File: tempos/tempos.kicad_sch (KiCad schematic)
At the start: 8 parts

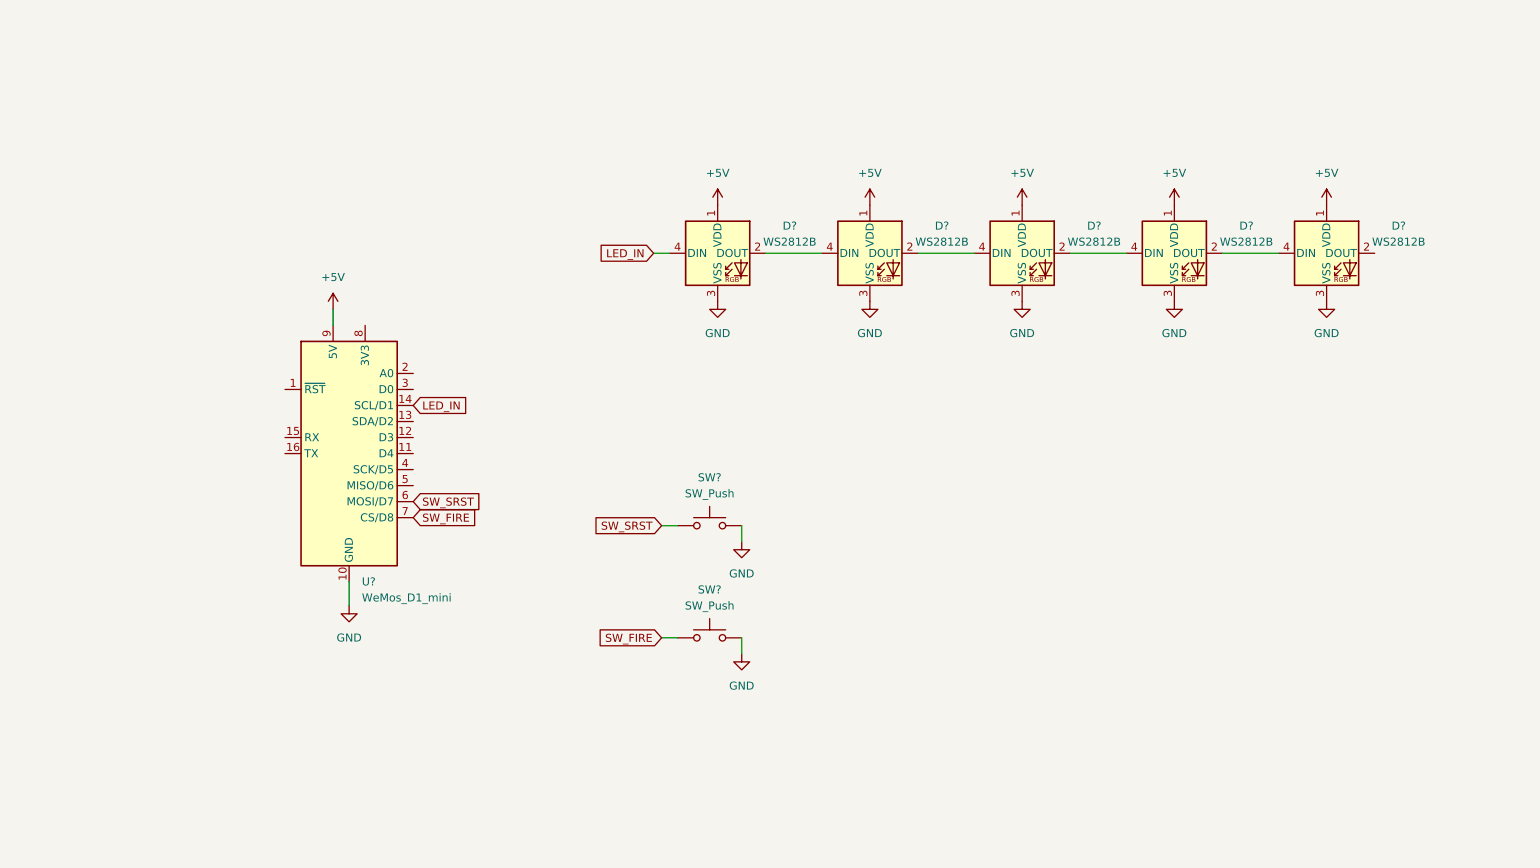
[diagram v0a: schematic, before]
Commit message: tempos: Transmission wire
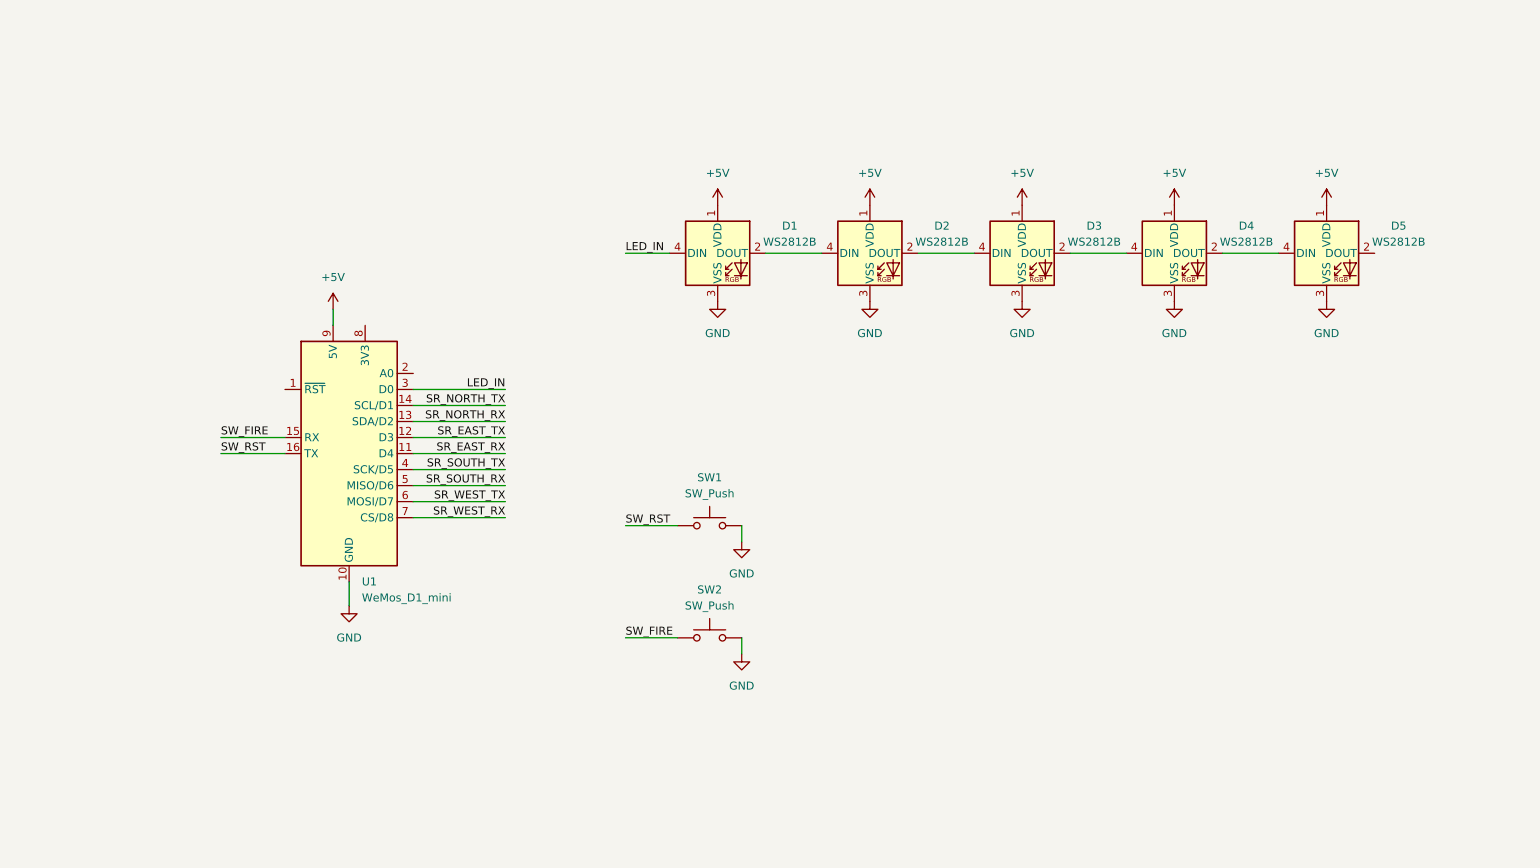
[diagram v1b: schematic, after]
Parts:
- gave numbers to parts that had none: 8
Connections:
- net LED_IN: now also U1.3 (D0); no longer U1.14 (SCL/D1)
- net SW_FIRE: now also U1.15 (RX); no longer U1.7 (CS/D8)
- net SR_EAST_RX: now reaches U1.11 (D4)
- net SR_EAST_TX: now reaches U1.12 (D3)
- net SR_NORTH_RX: now reaches U1.13 (SDA/D2)
- net SW_RST: now reaches U1.16 (TX)
- net SW_RST: now also SW1.1
- net SR_SOUTH_TX: now reaches U1.4 (SCK/D5)
- net SR_SOUTH_RX: now reaches U1.5 (MISO/D6)
- net SW_SRST renamed SR_WEST_TX
- net SR_WEST_TX: no longer SW1.1
- new net SR_NORTH_TX: U1.14 (SCL/D1)
- new net SR_WEST_RX: U1.7 (CS/D8)

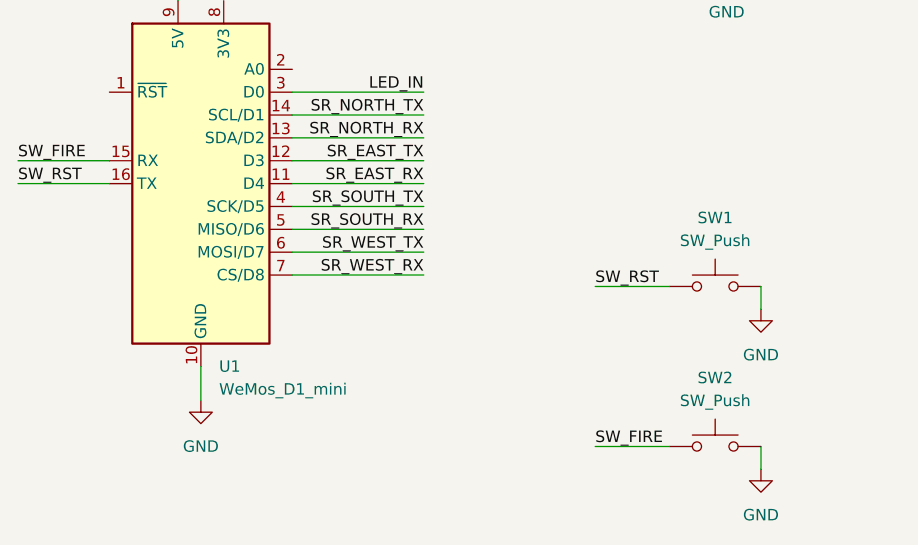
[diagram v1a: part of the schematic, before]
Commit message: tempos: Text description for the switches
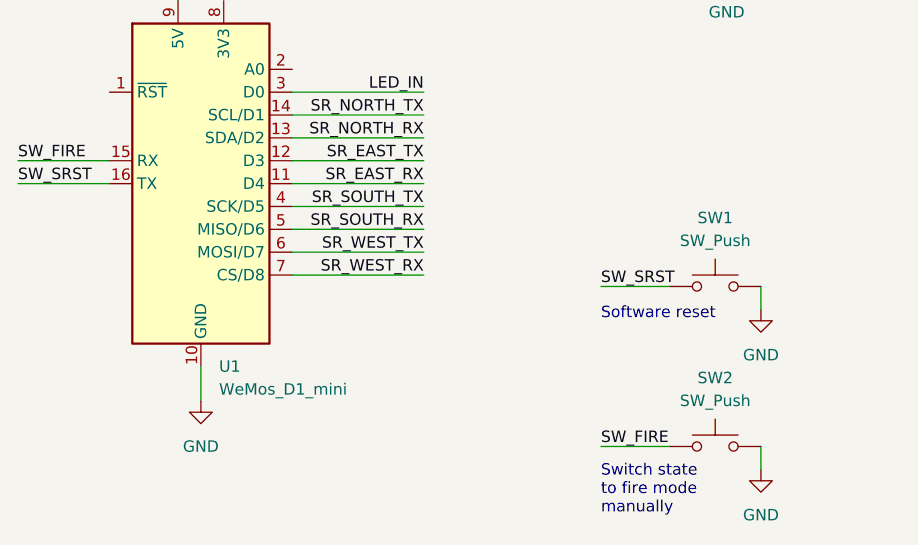
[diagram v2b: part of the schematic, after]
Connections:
- net SW_RST renamed SW_SRST
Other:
- note added: "Software reset"
- note added: "Switch state to fire mode manually"
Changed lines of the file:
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@@
     (stroke (width 0) (type default) (color 0 0 0 0))
   )
-  (wire (pts (xy 130.175 107.95) (xy 138.43 107.95))
+  (wire (pts (xy 130.81 107.95) (xy 138.43 107.95))
     (stroke (width 0) (type default) (color 0 0 0 0))
   )
@@
     (stroke (width 0) (type default) (color 0 0 0 0))
   )
-  (wire (pts (xy 130.175 125.73) (xy 138.43 125.73))
+  (wire (pts (xy 130.81 125.73) (xy 138.43 125.73))
     (stroke (width 0) (type default) (color 0 0 0 0))
+  )
+  (text "Switch state\nto fire mode\nmanually" (at 130.81 133.35 0)
+    (effects (font (size 1.27 1.27)) (justify left bottom))
+  )
+  (text "Software reset" (at 130.81 111.76 0)
+    (effects (font (size 1.27 1.27)) (justify left bottom))
   )
   (label "SR_WEST_TX" (at 111.125 104.14 180)
@@
     (effects (font (size 1.27 1.27)) (justify right bottom))
   )
-  (label "SW_RST" (at 66.04 96.52 0)
+  (label "SW_SRST" (at 66.04 96.52 0)
     (effects (font (size 1.27 1.27)) (justify left bottom))
   )
@@
     (effects (font (size 1.27 1.27)) (justify right bottom))
   )
-  (label "SW_FIRE" (at 130.175 125.73 0)
+  (label "SW_FIRE" (at 130.81 125.73 0)
     (effects (font (size 1.27 1.27)) (justify left bottom))
   )
@@
     (effects (font (size 1.27 1.27)) (justify right bottom))
   )
-  (label "SW_RST" (at 130.175 107.95 0)
+  (label "SW_SRST" (at 130.81 107.95 0)
     (effects (font (size 1.27 1.27)) (justify left bottom))
   )

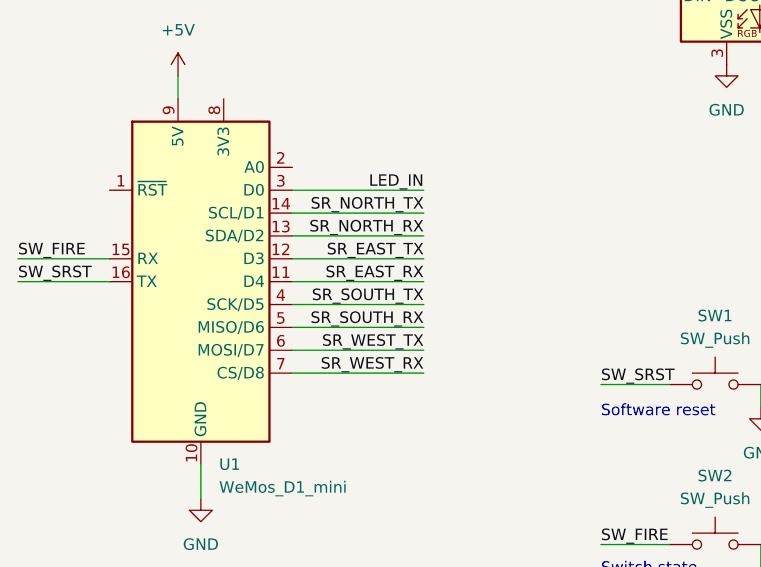
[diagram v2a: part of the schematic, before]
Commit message: tempos: Rearrange RX/TX pins
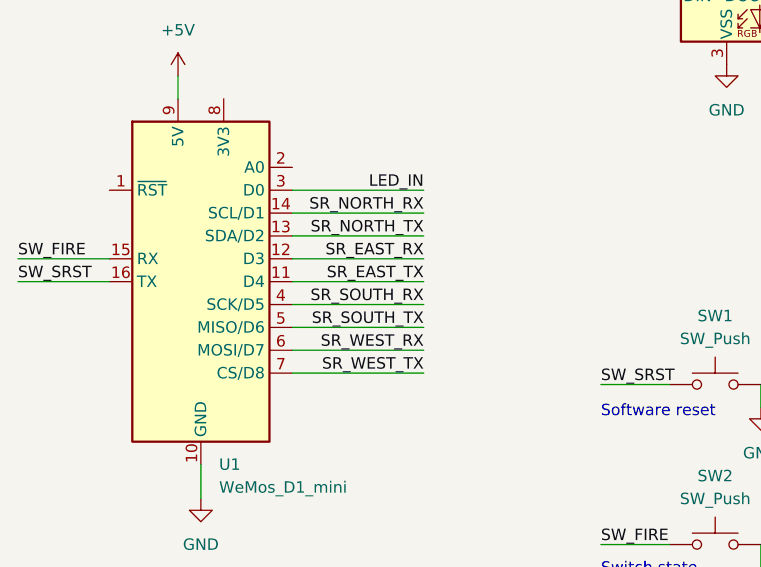
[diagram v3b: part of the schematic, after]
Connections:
- net SR_EAST_RX: now also U1.12 (D3); no longer U1.11 (D4)
- net SR_EAST_TX: now also U1.11 (D4); no longer U1.12 (D3)
- net SR_NORTH_RX: now also U1.14 (SCL/D1); no longer U1.13 (SDA/D2)
- net SR_NORTH_TX: now also U1.13 (SDA/D2); no longer U1.14 (SCL/D1)
- net SR_SOUTH_RX: now also U1.4 (SCK/D5); no longer U1.5 (MISO/D6)
- net SR_SOUTH_TX: now also U1.5 (MISO/D6); no longer U1.4 (SCK/D5)
- net SR_WEST_RX: now also U1.6 (MOSI/D7); no longer U1.7 (CS/D8)
- net SR_WEST_TX: now also U1.7 (CS/D8); no longer U1.6 (MOSI/D7)
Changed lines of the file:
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@@
     (effects (font (size 1.27 1.27)) (justify left bottom))
   )
-  (label "SR_WEST_TX" (at 111.125 104.14 180)
+  (label "SR_WEST_RX" (at 111.125 104.14 180)
     (effects (font (size 1.27 1.27)) (justify right bottom))
   )
-  (label "SR_EAST_TX" (at 111.125 93.98 180)
+  (label "SR_EAST_RX" (at 111.125 93.98 180)
     (effects (font (size 1.27 1.27)) (justify right bottom))
   )
-  (label "SR_NORTH_RX" (at 111.125 91.44 180)
+  (label "SR_NORTH_TX" (at 111.125 91.44 180)
     (effects (font (size 1.27 1.27)) (justify right bottom))
   )
@@
     (effects (font (size 1.27 1.27)) (justify left bottom))
   )
-  (label "SR_WEST_RX" (at 111.125 106.68 180)
+  (label "SR_WEST_TX" (at 111.125 106.68 180)
     (effects (font (size 1.27 1.27)) (justify right bottom))
   )
@@
     (effects (font (size 1.27 1.27)) (justify left bottom))
   )
-  (label "SR_SOUTH_TX" (at 111.125 99.06 180)
+  (label "SR_SOUTH_RX" (at 111.125 99.06 180)
     (effects (font (size 1.27 1.27)) (justify right bottom))
   )
-  (label "SR_NORTH_TX" (at 111.125 88.9 180)
+  (label "SR_NORTH_RX" (at 111.125 88.9 180)
     (effects (font (size 1.27 1.27)) (justify right bottom))
   )
@@
     (effects (font (size 1.27 1.27)) (justify left bottom))
   )
-  (label "SR_EAST_RX" (at 111.125 96.52 180)
+  (label "SR_EAST_TX" (at 111.125 96.52 180)
     (effects (font (size 1.27 1.27)) (justify right bottom))
   )
-  (label "SR_SOUTH_RX" (at 111.125 101.6 180)
+  (label "SR_SOUTH_TX" (at 111.125 101.6 180)
     (effects (font (size 1.27 1.27)) (justify right bottom))
   )

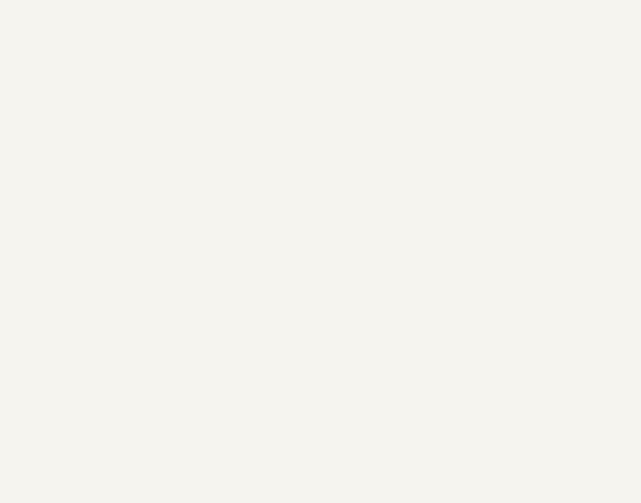
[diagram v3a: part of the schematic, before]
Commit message: hardware: Circuit diagram for six nodes  Connected RX/TX pins together between six nodes.
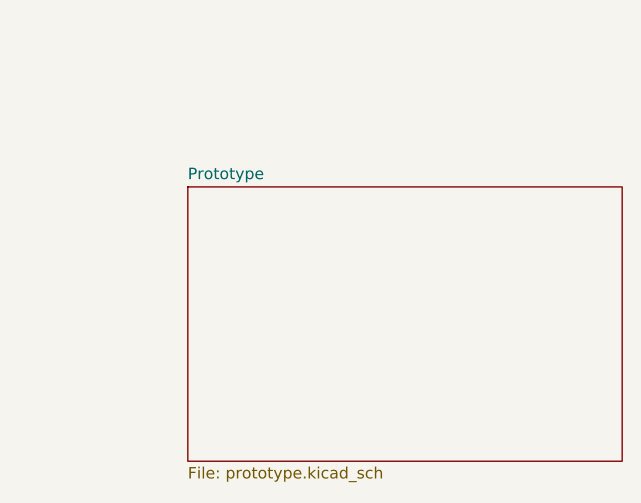
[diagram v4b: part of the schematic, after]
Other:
- added sheet Prototype (prototype.kicad_sch)
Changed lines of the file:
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@@
     (pin "2")
+  )
+  (sheet (at 224.79 127) (size 48.26 30.48) (fields_autoplaced)
+    (stroke (width 0.1524) (type solid) (color 0 0 0 0))
+    (fill (color 0 0 0 0.0000))
+    (property "Sheet name" "Prototype" (id 0) (at 224.79 126.2884 0)
+      (effects (font (size 1.27 1.27)) (justify left bottom))
+    )
+    (property "Sheet file" "prototype.kicad_sch" (id 1) (at 224.79 158.0646 0)
+      (effects (font (size 1.27 1.27)) (justify left top))
+    )
   )
   (sheet_instances
     (path "/" (page "1"))
+    (path "/2c19c399-c4f7-40ce-804e-49fc3383ca4e" (page "2"))
   )
   (symbol_instances
@@
       (reference "#PWR014") (unit 1) (value "GND") (footprint "")
     )
+    (path "/2c19c399-c4f7-40ce-804e-49fc3383ca4e/3c29d72d-e391-4942-8469-a1a227f3d93d"
+      (reference "#PWR?") (unit 1) (value "GND") (footprint "")
+    )
+    (path "/2c19c399-c4f7-40ce-804e-49fc3383ca4e/3d046c0b-d445-4332-a8e3-cad08dc3d7a5"
+      (reference "#PWR?") (unit 1) (value "GND") (footprint "")
+    )
+    (path "/2c19c399-c4f7-40ce-804e-49fc3383ca4e/4f84264e-389c-4cb3-b1ef-b18c33e26c32"
+      (reference "#PWR?") (unit 1) (value "GND") (footprint "")
+    )
+    (path "/2c19c399-c4f7-40ce-804e-49fc3383ca4e/684ab4bf-d763-4862-8762-c7424275837e"
+      (reference "#PWR?") (unit 1) (value "+3.3V") (footprint "")
+    )
+    (path "/2c19c399-c4f7-40ce-804e-49fc3383ca4e/6ef3b29a-ee7a-4b63-81c1-ce6ddc24bb1c"
+      (reference "#PWR?") (unit 1) (value "GND") (footprint "")
+    )
+    (path "/2c19c399-c4f7-40ce-804e-49fc3383ca4e/6f3c1782-d190-44d6-b32b-e4547d6c973b"
+      (reference "#PWR?") (unit 1) (value "+3.3V") (footprint "")
+    )
+    (path "/2c19c399-c4f7-40ce-804e-49fc3383ca4e/7c97b1c9-4321-4174-981f-9646edd3dcd6"
+      (reference "#PWR?") (unit 1) (value "+3.3V") (footprint "")
+    )
+    (path "/2c19c399-c4f7-40ce-804e-49fc3383ca4e/98a4c6aa-259e-4081-9383-2e60646be403"
+      (reference "#PWR?") (unit 1) (value "+3.3V") (footprint "")
+    )
+    (path "/2c19c399-c4f7-40ce-804e-49fc3383ca4e/bb7f49a8-37a0-4430-adfe-10237aaa0106"
+      (reference "#PWR?") (unit 1) (value "+3.3V") (footprint "")
+    )
+    (path "/2c19c399-c4f7-40ce-804e-49fc3383ca4e/bcbec452-6f24-4fa2-bcf6-898df827344a"
+      (reference "#PWR?") (unit 1) (value "+3.3V") (footprint "")
+    )
+    (path "/2c19c399-c4f7-40ce-804e-49fc3383ca4e/fa4fd627-4259-4330-bbdf-3673be9bdffd"
+      (reference "#PWR?") (unit 1) (value "GND") (footprint "")
+    )
+    (path "/2c19c399-c4f7-40ce-804e-49fc3383ca4e/fe72663a-120a-4556-9cd5-6bd60258b464"
+      (reference "#PWR?") (unit 1) (value "GND") (footprint "")
+    )
     (path "/eb30ba93-4b30-413b-b3b4-5dbe10cd6f18"
       (reference "D1") (unit 1) (value "WS2812B") (footprint "")
@@
       (reference "U1") (unit 1) (value "WeMos_D1_mini") (footprint "Module:WEMOS_D1_mini_light")
     )
+    (path "/2c19c399-c4f7-40ce-804e-49fc3383ca4e/2ac05e0a-a519-4fbd-a00c-2a5e9f9d000c"
+      (reference "U?") (unit 1) (value "WeMos_D1_mini") (footprint "Module:WEMOS_D1_mini_light")
+    )
+    (path "/2c19c399-c4f7-40ce-804e-49fc3383ca4e/3e6f4211-8543-4b21-8501-727ffb144cf7"
+      (reference "U?") (unit 1) (value "WeMos_D1_mini") (footprint "Module:WEMOS_D1_mini_light")
+    )
+    (path "/2c19c399-c4f7-40ce-804e-49fc3383ca4e/8721c7ed-7c2e-44cf-992d-79845ff9e4f2"
+      (reference "U?") (unit 1) (value "WeMos_D1_mini") (footprint "Module:WEMOS_D1_mini_light")
+    )
+    (path "/2c19c399-c4f7-40ce-804e-49fc3383ca4e/af3a251f-83a0-463a-a803-386022e5f023"
+      (reference "U?") (unit 1) (value "WeMos_D1_mini") (footprint "Module:WEMOS_D1_mini_light")
+    )
+    (path "/2c19c399-c4f7-40ce-804e-49fc3383ca4e/d19099b9-5143-4ebb-b89a-345660ee0eeb"
+      (reference "U?") (unit 1) (value "WeMos_D1_mini") (footprint "Module:WEMOS_D1_mini_light")
+    )
+    (path "/2c19c399-c4f7-40ce-804e-49fc3383ca4e/e6e355cc-e4e4-4b24-8b96-bd6fb26a2961"
+      (reference "U?") (unit 1) (value "WeMos_D1_mini") (footprint "Module:WEMOS_D1_mini_light")
+    )
   )
